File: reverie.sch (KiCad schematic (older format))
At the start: 141 parts, among them SW1 SW_Push, U1 PRTR5V0U2X, U2 ATmega32U4-AU, Y1 16MHz

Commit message: initial layout and routing
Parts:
- removed R5, R6: 22, Resistor_SMD:R_0805_2012Metric, symbol Device:R_Small
- C1, C2: value 22uF -> 22pF
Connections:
- net VCC is gone; now on net +5V: F1.1
- net +5V: now also R1.2, U2.14 (VCC), U2.2 (UVCC), U2.24 (AVCC), U2.34 (VCC), U2.44 (AVCC)
- net D+: now also U2.4 (D+)
- net D-: now also U2.3 (D-)
- net GND: now also U1.1 (GND)
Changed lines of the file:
@@
 L power:+5V #PWR0101
 U 1 1 5EC3411F
-P 2600 3500
-F 0 "#PWR0101" H 2600 3350 50  0001 C CNN
-F 1 "+5V" H 2615 3673 50  0000 C CNN
-F 2 "" H 2600 3500 50  0001 C CNN
-F 3 "" H 2600 3500 50  0001 C CNN
-	1    2600 3500
+P 2650 3500
+F 0 "#PWR0101" H 2650 3350 50  0001 C CNN
+F 1 "+5V" H 2665 3673 50  0000 C CNN
+F 2 "" H 2650 3500 50  0001 C CNN
+F 3 "" H 2650 3500 50  0001 C CNN
+	1    2650 3500
 	1    0    0    -1
 $EndComp
@@
 $EndComp
 $Comp
-L Device:R_Small R5
-U 1 1 5EC3B403
-P 1600 5050
-F 0 "R5" V 1404 5050 50  0000 C CNN
-F 1 "22" V 1495 5050 50  0000 C CNN
-F 2 "Resistor_SMD:R_0805_2012Metric" H 1600 5050 50  0001 C CNN
-F 3 "~" H 1600 5050 50  0001 C CNN
-	1    1600 5050
-	0    1    1    0
-$EndComp
-$Comp
-L Device:R_Small R6
-U 1 1 5EC3C6E4
-P 1200 5150
-F 0 "R6" V 1004 5150 50  0000 C CNN
-F 1 "22" V 1095 5150 50  0000 C CNN
-F 2 "Resistor_SMD:R_0805_2012Metric" H 1200 5150 50  0001 C CNN
-F 3 "~" H 1200 5150 50  0001 C CNN
-	1    1200 5150
-	0    1    1    0
-$EndComp
-Wire Wire Line
-	2150 5050 1700 5050
-Wire Wire Line
-	2150 5150 1300 5150
-Wire Wire Line
-	1500 5050 800  5050
-Wire Wire Line
-	1100 5150 800  5150
-$Comp
 L Device:C_Small C3
 U 1 1 5EC3E35C
@@
 P 800 4150
 F 0 "C1" V 571 4150 50  0000 C CNN
-F 1 "22uF" V 662 4150 50  0000 C CNN
+F 1 "22pF" V 662 4150 50  0000 C CNN
 F 2 "Capacitor_SMD:C_0805_2012Metric" H 800 4150 50  0001 C CNN
 F 3 "~" H 800 4150 50  0001 C CNN
@@
 P 800 4600
 F 0 "C2" V 571 4600 50  0000 C CNN
-F 1 "22uF" V 662 4600 50  0000 C CNN
+F 1 "22pF" V 662 4600 50  0000 C CNN
 F 2 "Capacitor_SMD:C_0805_2012Metric" H 800 4600 50  0001 C CNN
 F 3 "~" H 800 4600 50  0001 C CNN
@@
 	2650 3500 2650 3550
 Wire Wire Line
-	2850 3750 2750 3750
-Wire Wire Line
 	2750 3750 2650 3750
-Connection ~ 2750 3750
 Connection ~ 2650 3750
 Wire Wire Line
@@
 	10700 800  10700 1150
 Connection ~ 10700 1150
-Wire Wire Line
-	11150 800  11150 1150
 $Comp
 L Type-C:HRO-TYPE-C-31-M-12 USB1
@@
 Wire Wire Line
 	5850 4400 5800 4400
-$Comp
-L power:VCC #PWR0111
-U 1 1 5F0AC5CF
-P 6500 4400
-F 0 "#PWR0111" H 6500 4250 50  0001 C CNN
-F 1 "VCC" H 6517 4573 50  0000 C CNN
-F 2 "" H 6500 4400 50  0001 C CNN
-F 3 "" H 6500 4400 50  0001 C CNN
-	1    6500 4400
-	1    0    0    -1
-$EndComp
 Wire Wire Line
 	6500 4400 6050 4400
@@
 	5850 4800 5850 4900
 Wire Wire Line
-	7500 5150 7500 5300
-Wire Wire Line
-	7500 5300 6950 5300
-Wire Wire Line
-	6950 5300 6950 4650
+	7500 5150 7500 5200
 Wire Wire Line
 	6950 4650 6400 4650
@@
 Wire Wire Line
 	5100 2650 5000 2650
+$Comp
+L power:GND #PWR0114
+U 1 1 5EC6D949
+P 7400 5250
+F 0 "#PWR0114" H 7400 5000 50  0001 C CNN
+F 1 "GND" H 7405 5077 50  0000 C CNN
+F 2 "" H 7400 5250 50  0001 C CNN
+F 3 "" H 7400 5250 50  0001 C CNN
+	1    7400 5250
+	1    0    0    -1
+$EndComp
+Wire Wire Line
+	7500 5200 6950 5200
+Wire Wire Line
+	6950 5200 6950 4650
+Wire Wire Line
+	7400 5150 7400 5250
+Wire Wire Line
+	2850 3750 2750 3750
+Connection ~ 2750 3750
+Wire Wire Line
+	11150 800  11150 1150
+Wire Wire Line
+	800  5150 2150 5150
+Wire Wire Line
+	800  5050 2150 5050
+$Comp
+L power:+5V #PWR?
+U 1 1 5EE61113
+P 6500 4400
+F 0 "#PWR?" H 6500 4250 50  0001 C CNN
+F 1 "+5V" H 6515 4573 50  0000 C CNN
+F 2 "" H 6500 4400 50  0001 C CNN
+F 3 "" H 6500 4400 50  0001 C CNN
+	1    6500 4400
+	1    0    0    -1
+$EndComp
 $EndSCHEMATC

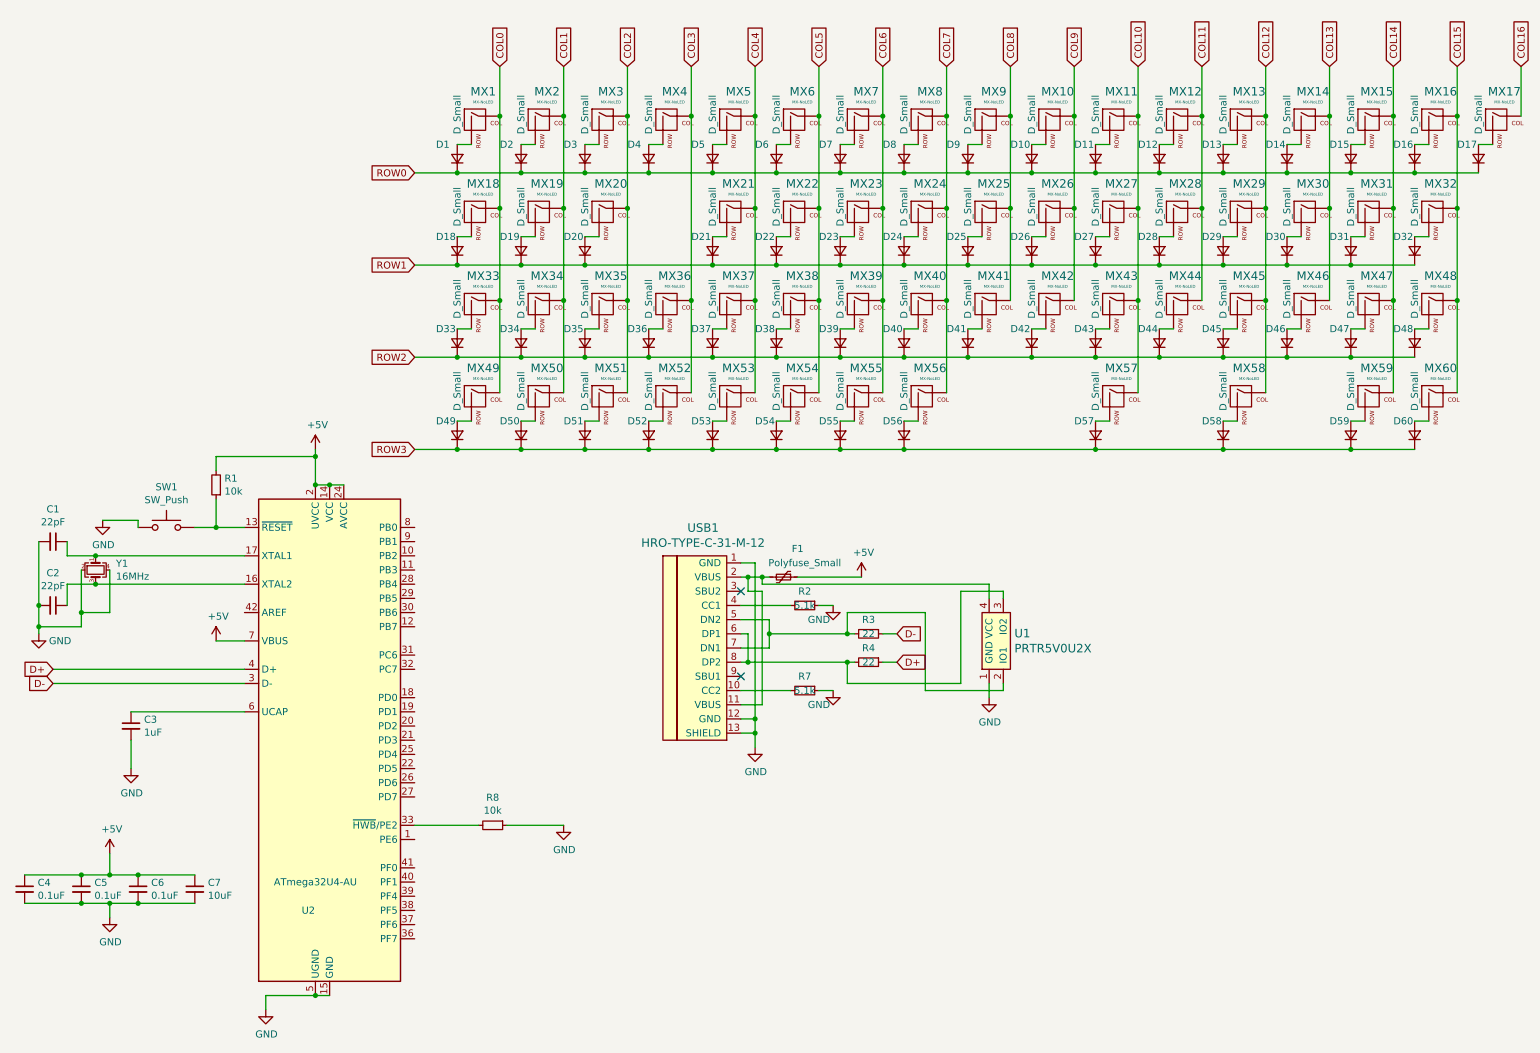
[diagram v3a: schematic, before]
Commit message: complete routing
add ISP programmer
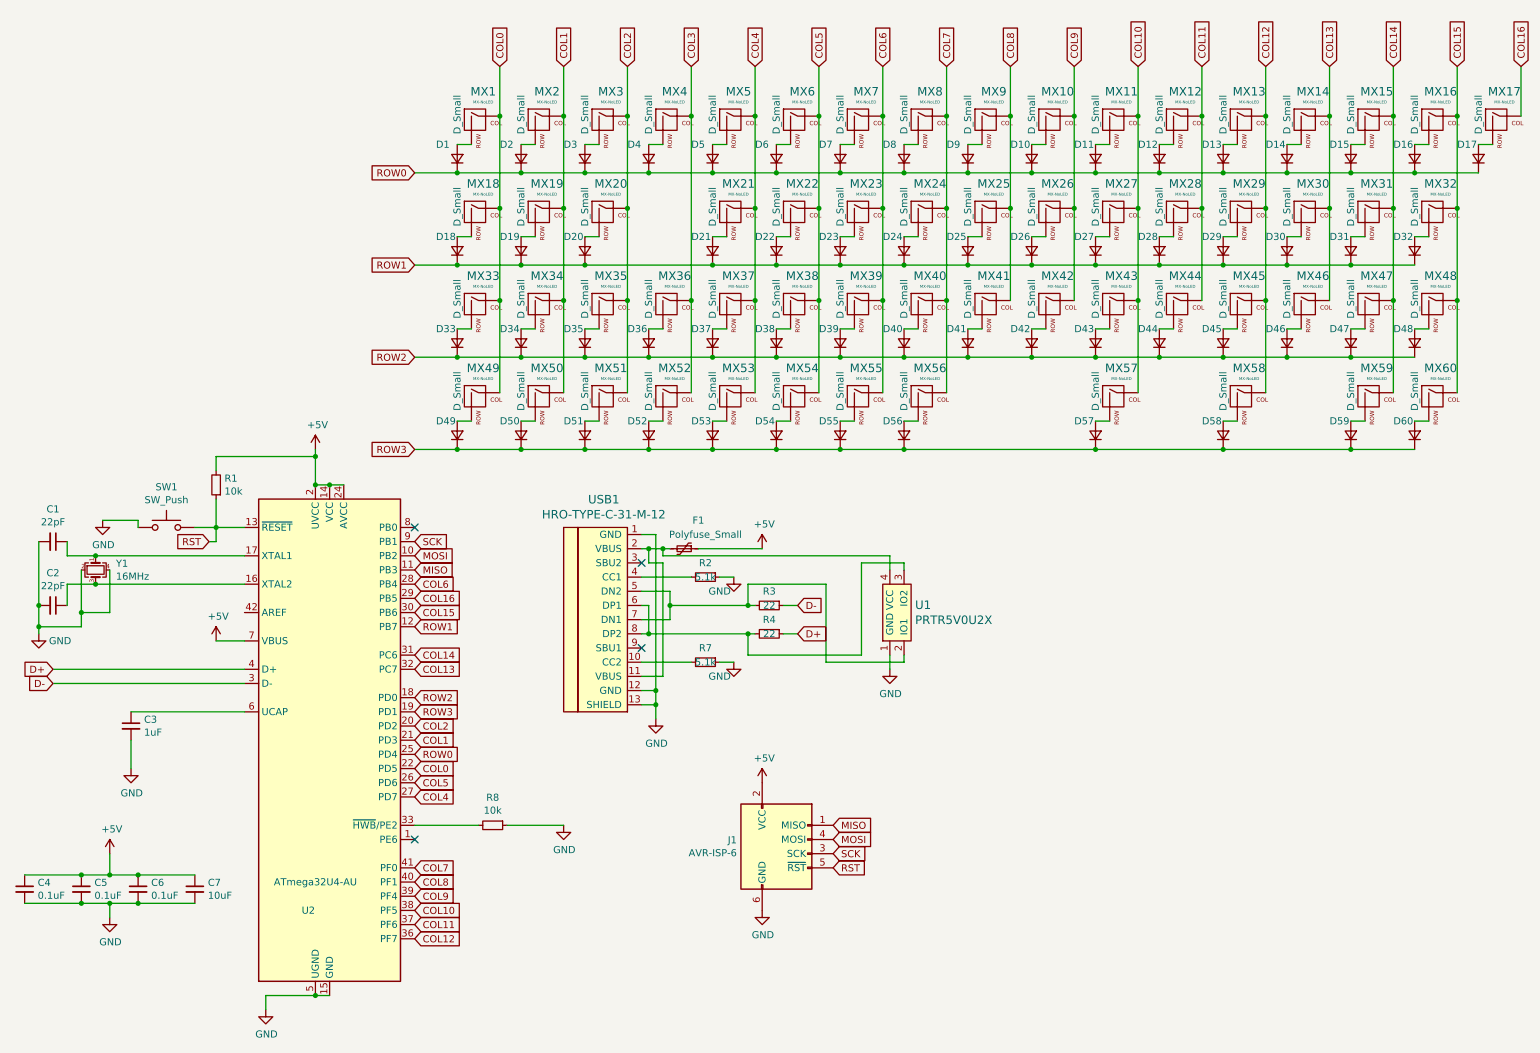
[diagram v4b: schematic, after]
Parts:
- added J1: AVR-ISP-6, Connector_IDC:IDC-Header_2x03_P2.54mm_Vertical, symbol Connector:AVR-ISP-6
- MX56: footprint MX_Only:MXOnly-2.25U-Hotswap -> MX_Only:MXOnly-2.25U-Hotswap-ReversedStabilizers
- MX57: footprint MX_Only:MXOnly-2.75U-Hotswap -> MX_Only:MXOnly-2.75U-Hotswap-ReversedStabilizers
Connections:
- net +5V: now also J1.2 (VCC)
- net COL0: now also U2.22 (PD5)
- net COL1: now also U2.21 (PD3)
- net COL10: now also U2.38 (PF5)
- net COL11: now also U2.37 (PF6)
- net COL12: now also U2.36 (PF7)
- net COL13: now also U2.32 (PC7)
- net COL14: now also U2.31 (PC6)
- net COL15: now also U2.30 (PB6)
- net COL16: now also U2.29 (PB5)
- net COL2: now also U2.20 (PD2)
- net COL4: now also U2.27 (PD7)
- net COL5: now also U2.26 (PD6)
- net COL6: now also U2.28 (PB4)
- net COL7: now also U2.41 (PF0)
- net COL8: now also U2.40 (PF1)
- net COL9: now also U2.39 (PF4)
- net GND: now also J1.6 (GND)
- net ROW0: now also U2.25 (PD4)
- net ROW1: now also U2.12 (PB7)
- net ROW2: now also U2.18 (PD0)
- net ROW3: now also U2.19 (PD1)
- net MOSI: now reaches U2.10 (PB2)
- net MOSI: now also J1.4 (MOSI)
- net MISO: now reaches U2.11 (PB3)
- net MISO: now also J1.1 (MISO)
- net RST: now reaches R1.1, SW1.2, U2.13 (~RESET)
- net RST: now also J1.5 (~RST)
- net SCK: now reaches U2.9 (PB1)
- net SCK: now also J1.3 (SCK)
- no-connect marks 2 -> 4
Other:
- moved on the sheet: F1, R2, R3, R4, R7, U1, USB1

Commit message: clean up
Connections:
- net COL3: now also U2.8 (PB0)
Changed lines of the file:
@@
 	1    0    0    -1
 $EndComp
-Wire Wire Line
-	1950 4850 2150 4850
 $Comp
 L Device:Crystal_GND24_Small Y1
@@
 Wire Wire Line
 	1950 4150 1950 4050
-NoConn ~ 3350 4050
 NoConn ~ 3350 6250
+NoConn ~ 2150 4650
+Text GLabel 3350 4050 2    50   Input ~ 0
+COL3
+Wire Wire Line
+	2150 4850 1950 4850
 $EndSCHEMATC

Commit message: work on edgecuts and replace isp footprint
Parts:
- J1: footprint Connector_IDC:IDC-Header_2x03_P2.54mm_Vertical -> random-keyboard-parts:Reset_Pretty-Mask
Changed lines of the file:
@@
 F 0 "J1" H 5621 6446 50  0000 R CNN
 F 1 "AVR-ISP-6" H 5621 6355 50  0000 R CNN
-F 2 "Connector_IDC:IDC-Header_2x03_P2.54mm_Vertical" V 5650 6400 50  0001 C CNN
+F 2 "random-keyboard-parts:Reset_Pretty-Mask" V 5650 6400 50  0001 C CNN
 F 3 " ~" H 4625 5800 50  0001 C CNN
 	1    5900 6350
